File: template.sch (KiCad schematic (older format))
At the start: 24 parts, among them J1 power, J2 input, J3 output, J4 isp, K1 EC2-5NU, K2 EC2-5NU, K3 EC2-5NU, SW1 bypass switch, SW2 preset switch, U1 AMS1117-5.0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

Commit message: Lots of progress
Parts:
- D2, D3: footprint LED_THT:LED_D5.0mm -> LED_THT:LED_D5.0mm_compact
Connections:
- net 5V: now also K2.9; no longer K3.9
- net preset_2_in: now also K3.9; no longer K2.9
- net preset_2_out_a: now also K3.10; no longer K2.10
- net preset_2_out_b: now also K3.8; no longer K2.8
- net preset_led: now also K2.8; no longer K3.8
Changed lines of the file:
@@
 Text Label 4950 3250 0    50   ~ 0
 preset_switch
-Text Label 2100 7450 0    50   ~ 0
+Text Label 2100 6000 0    50   ~ 0
 preset_led
 Text Label 4950 3450 0    50   ~ 0
@@
 Text Label 1200 5500 2    50   ~ 0
 preset_1_in
-Text Label 1200 5900 2    50   ~ 0
+Text Label 1200 7350 2    50   ~ 0
 preset_2_in
 Wire Wire Line
 	1200 5500 1350 5500
 Wire Wire Line
-	1200 5900 1350 5900
+	1200 7350 1350 7350
 Text Label 10200 5200 0    50   ~ 0
 preset_1_in
@@
 	1200 6950 1350 6950
 Wire Wire Line
-	1200 7350 1350 7350
-Wire Wire Line
-	2100 7450 1950 7450
-NoConn ~ 1950 7250
+	1200 5900 1350 5900
+Wire Wire Line
+	2100 6000 1950 6000
+NoConn ~ 1950 5800
 Text Label 2100 7050 0    50   ~ 0
 preset_3_out_b
@@
 Wire Wire Line
 	8700 5750 8850 5750
-Text Label 2100 6000 0    50   ~ 0
+Text Label 2100 7450 0    50   ~ 0
 preset_2_out_b
 Wire Wire Line
-	2100 6000 1950 6000
-Text Label 2100 5800 0    50   ~ 0
+	2100 7450 1950 7450
+Text Label 2100 7250 0    50   ~ 0
 preset_2_out_a
 Wire Wire Line
-	2100 5800 1950 5800
+	2100 7250 1950 7250
 Text Label 8700 5450 2    50   ~ 0
 preset_2_out_a
@@
 Wire Wire Line
 	8850 5150 8700 5150
-Text Label 1200 7350 2    50   ~ 0
+Text Label 1200 5900 2    50   ~ 0
 5V
 $Comp
@@
 F 0 "D2" H 8043 1045 50  0000 C CNN
 F 1 "bypass" H 8043 1136 50  0000 C CNN
-F 2 "LED_THT:LED_D5.0mm" H 8050 1300 50  0001 C CNN
+F 2 "LED_THT:LED_D5.0mm_compact" H 8050 1300 50  0001 C CNN
 F 3 "~" H 8050 1300 50  0001 C CNN
 	1    8050 1300
@@
 F 0 "D3" H 8043 1995 50  0000 C CNN
 F 1 "preset" H 8043 2086 50  0000 C CNN
-F 2 "LED_THT:LED_D5.0mm" H 8050 2250 50  0001 C CNN
+F 2 "LED_THT:LED_D5.0mm_compact" H 8050 2250 50  0001 C CNN
 F 3 "~" H 8050 2250 50  0001 C CNN
 	1    8050 2250

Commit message: Some layout improvements
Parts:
- SW1, SW2: footprint Connector_JST:JST_XH_B2B-XH-AM_1x02_P2.50mm_Vertical -> Connector_JST:JST_XH_B2B-XH-A_1x02_P2.50mm_Vertical
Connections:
- net preset_relay: now also U3.5 (gate2); no longer U4.5 (gate2)
- net relay_3: now also U3.3 (drain2); no longer U4.3 (drain2)
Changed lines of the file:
@@
 F 0 "SW1" H 9200 1535 50  0000 C CNN
 F 1 "bypass switch" H 9200 1444 50  0000 C CNN
-F 2 "Connector_JST:JST_XH_B2B-XH-AM_1x02_P2.50mm_Vertical" H 9200 1300 50  0001 C CNN
+F 2 "Connector_JST:JST_XH_B2B-XH-A_1x02_P2.50mm_Vertical" H 9200 1300 50  0001 C CNN
 F 3 "~" H 9200 1300 50  0001 C CNN
 	1    9200 1300
@@
 F 0 "SW2" H 9200 2485 50  0000 C CNN
 F 1 "preset switch" H 9200 2394 50  0000 C CNN
-F 2 "Connector_JST:JST_XH_B2B-XH-AM_1x02_P2.50mm_Vertical" H 9200 2250 50  0001 C CNN
+F 2 "Connector_JST:JST_XH_B2B-XH-A_1x02_P2.50mm_Vertical" H 9200 2250 50  0001 C CNN
 F 3 "~" H 9200 2250 50  0001 C CNN
 	1    9200 2250
@@
 Wire Wire Line
 	3750 5200 3850 5200
-NoConn ~ 3850 5300
-NoConn ~ 4450 5000
 Text Label 5650 5200 2    50   ~ 0
 preset_relay
-Wire Wire Line
-	5650 5200 5750 5200
-Wire Wire Line
-	5750 5200 5750 5300
-Wire Wire Line
-	5750 5300 5800 5300
-Connection ~ 5750 5200
-Wire Wire Line
-	5750 5200 5800 5200
 Text Label 6300 4900 1    50   ~ 0
 relay_2
@@
 	6300 4900 6300 5000
 Wire Wire Line
-	6400 4900 6400 5000
-Text Label 6400 4900 1    50   ~ 0
+	4450 4900 4450 5000
+Text Label 4450 4900 1    50   ~ 0
 relay_3
 $Comp
@@
 	1    0    0    -1
 $EndComp
+Text Label 3750 5300 2    50   ~ 0
+preset_relay
+Wire Wire Line
+	3850 5300 3750 5300
+Wire Wire Line
+	5650 5200 5800 5200
+NoConn ~ 6400 5000
+NoConn ~ 5800 5300
 $EndSCHEMATC

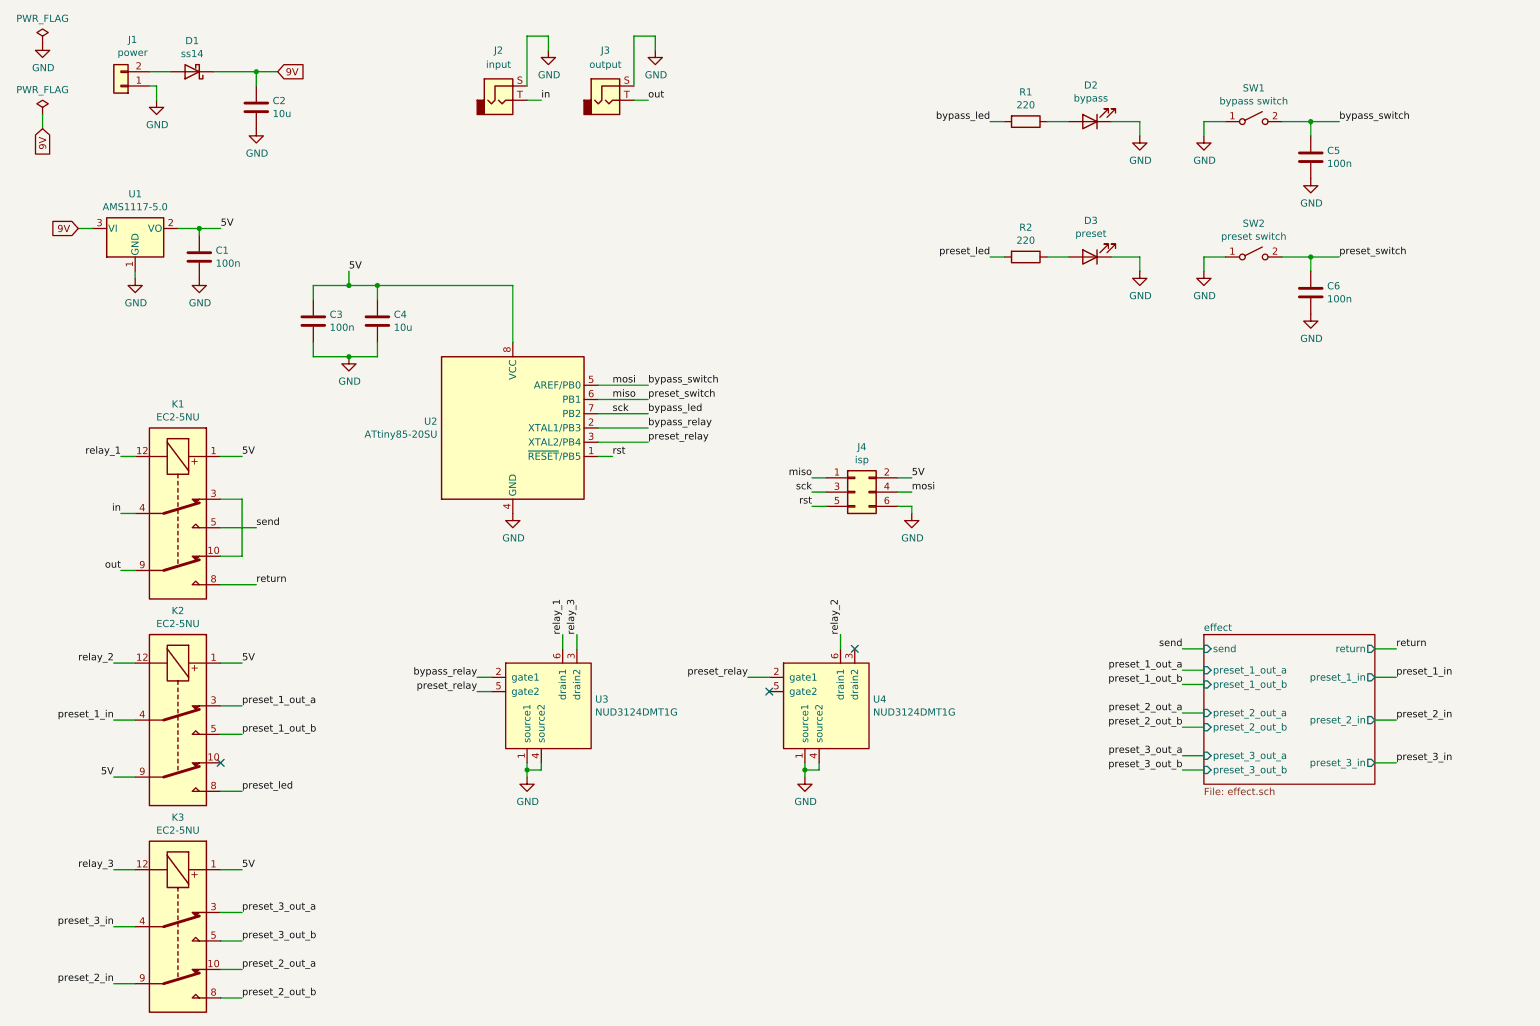
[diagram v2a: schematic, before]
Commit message: Use solid state switching and charge pump
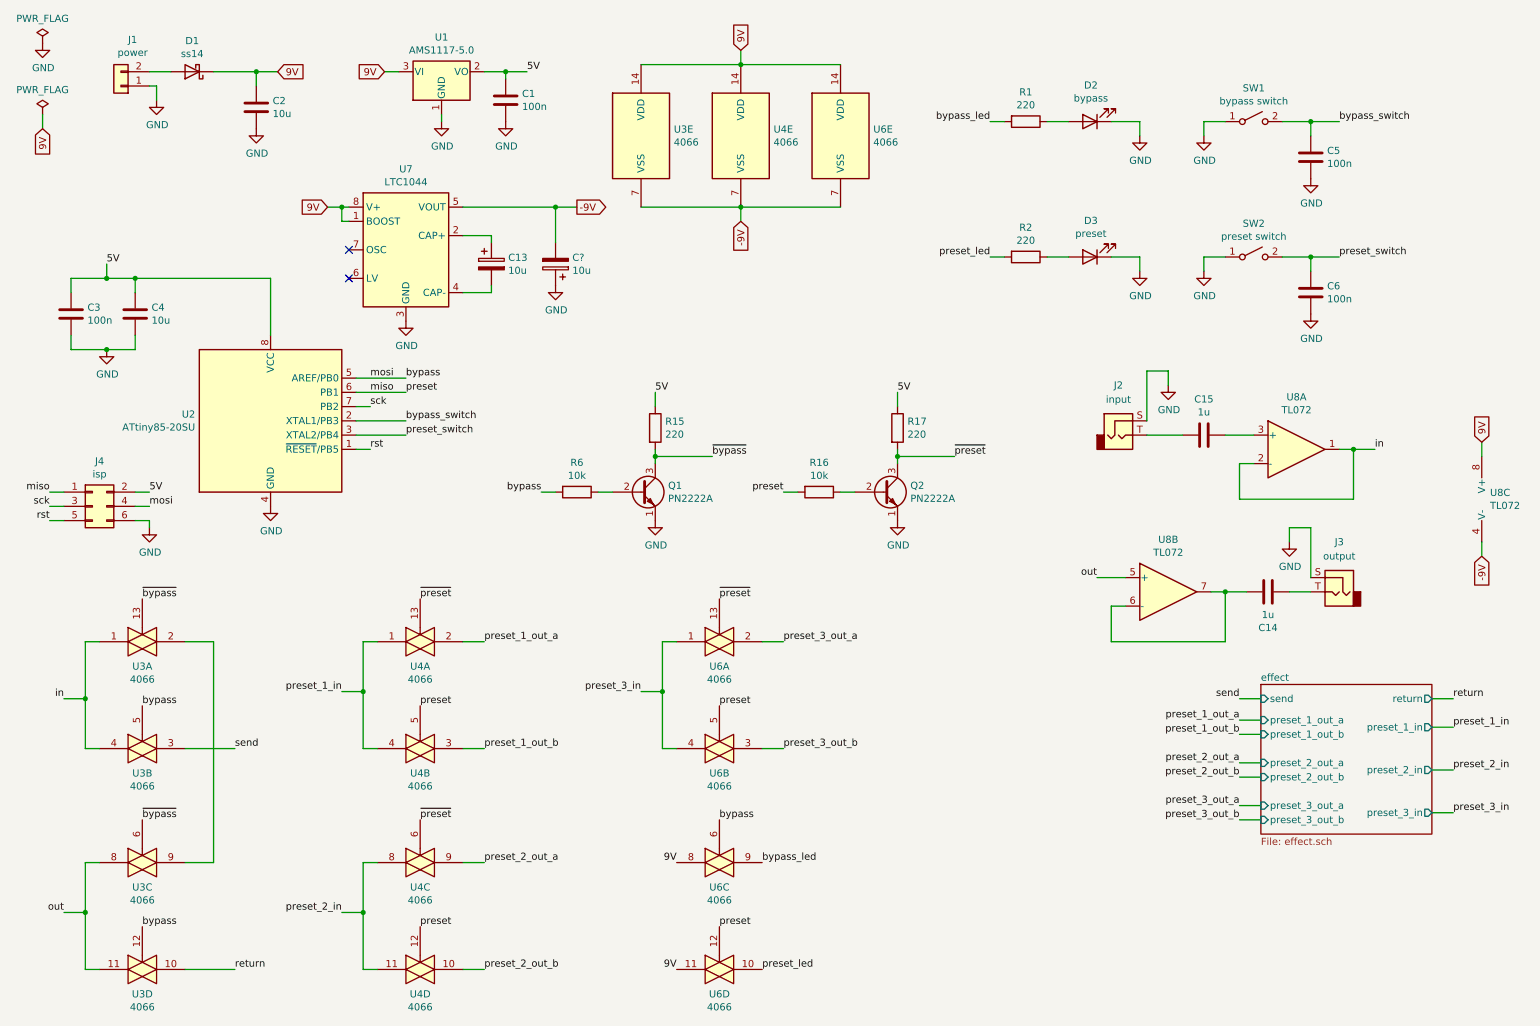
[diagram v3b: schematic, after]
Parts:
- removed K1, K2, K3: EC2-5NU, Relay_THT:Relay_DPDT_Kemet_EC2, symbol Relay:EC2-5NU
- removed U3, U4: NUD3124DMT1G, Package_SO:SC-74-6_1.5x2.9mm_P0.95mm, symbol Power_Management:NUD3124DMT1G
- added C13, C?: 10u, symbol Device:CP
- added C14, C15: 1u, symbol Device:C
- added Q1, Q2: PN2222A, Package_TO_SOT_THT:TO-92_Inline, symbol Transistor_BJT:PN2222A
- added R15, R17: 220, symbol Device:R
- added R16, R6: 10k, symbol Device:R
- added U3, U4, U6: 4066, symbol 4xxx:4066
- added U7: LTC1044, symbol Regulator_SwitchedCapacitor:LTC1044
- added U8: TL072, symbol Amplifier_Operational:TL072
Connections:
- net bypass_relay is gone; now on net bypass_switch: U2.2 (XTAL1/PB3)
- net 5V: now also R15.1, R17.1
- net 9V: now also U3.14 (VDD), U4.14 (VDD), U6.11, U6.14 (VDD), U6.8, U7.1 (BOOST), U7.8 (V+), U8.8 (V+)
- net GND: now also C?.1, Q1.1 (E), Q2.1 (E), U7.3 (GND)
- net bypass_led: now also U6.9; no longer J4.3 (Pin_3), U2.7 (PB2)
- net bypass_switch: no longer J4.4 (Pin_4), U2.5 (AREF/PB0)
- net in: now also U3.1, U3.4, U8.1, U8.2 (-); no longer J2.T
- net miso: now also R16.2, U4.12, U4.5, U6.12, U6.5; no longer C6.1, SW2.2 (B)
- net out: now also U3.11, U3.8, U8.5 (+); no longer J3.T
- net preset_1_in: now also U4.1, U4.4
- net preset_1_out_a: now also U4.2
- net preset_1_out_b: now also U4.3
- net preset_2_in: now also U4.11, U4.8
- net preset_2_out_a: now also U4.9
- net preset_2_out_b: now also U4.10
- net preset_3_in: now also U6.1, U6.4
- net preset_3_out_a: now also U6.2
- net preset_3_out_b: now also U6.3
- net preset_led: now also U6.10
- net return: now also U3.10
- net send: now also U3.3
- net preset_relay renamed preset_switch
- net preset_switch: now also C6.1, SW2.2 (B)
- new net: C15.2, J2.T
- new net: C14.2, J3.T
- new net: U3.2, U3.9
- new net: Q1.2 (B), R6.1
- new net: Q2.2 (B), R16.1
- new net: C14.1, U8.6 (-), U8.7
- new net: C15.1, U8.3 (+)
- new net: C13.1, U7.2 (CAP+)
- new net: C13.2, U7.4 (CAP-)
- new net -9V: C?.2, U3.7 (VSS), U4.7 (VSS), U6.7 (VSS), U7.5 (VOUT), U8.4 (V-)
- new net bypass: J4.4 (Pin_4), R6.2, U2.5 (AREF/PB0), U3.12, U3.5, U6.6
- new net sck: J4.3 (Pin_3), U2.7 (PB2)
- new net ~bypass: Q1.3 (C), R15.2, U3.13, U3.6
- new net ~preset: Q2.3 (C), R17.2, U4.13, U4.6, U6.13
- no-connect marks 3 -> 2
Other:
- moved on the sheet: C1, C3, C4, J2, J3, J4, U1, U2

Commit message: Use 4053 switch, correct poor decisions made earlier
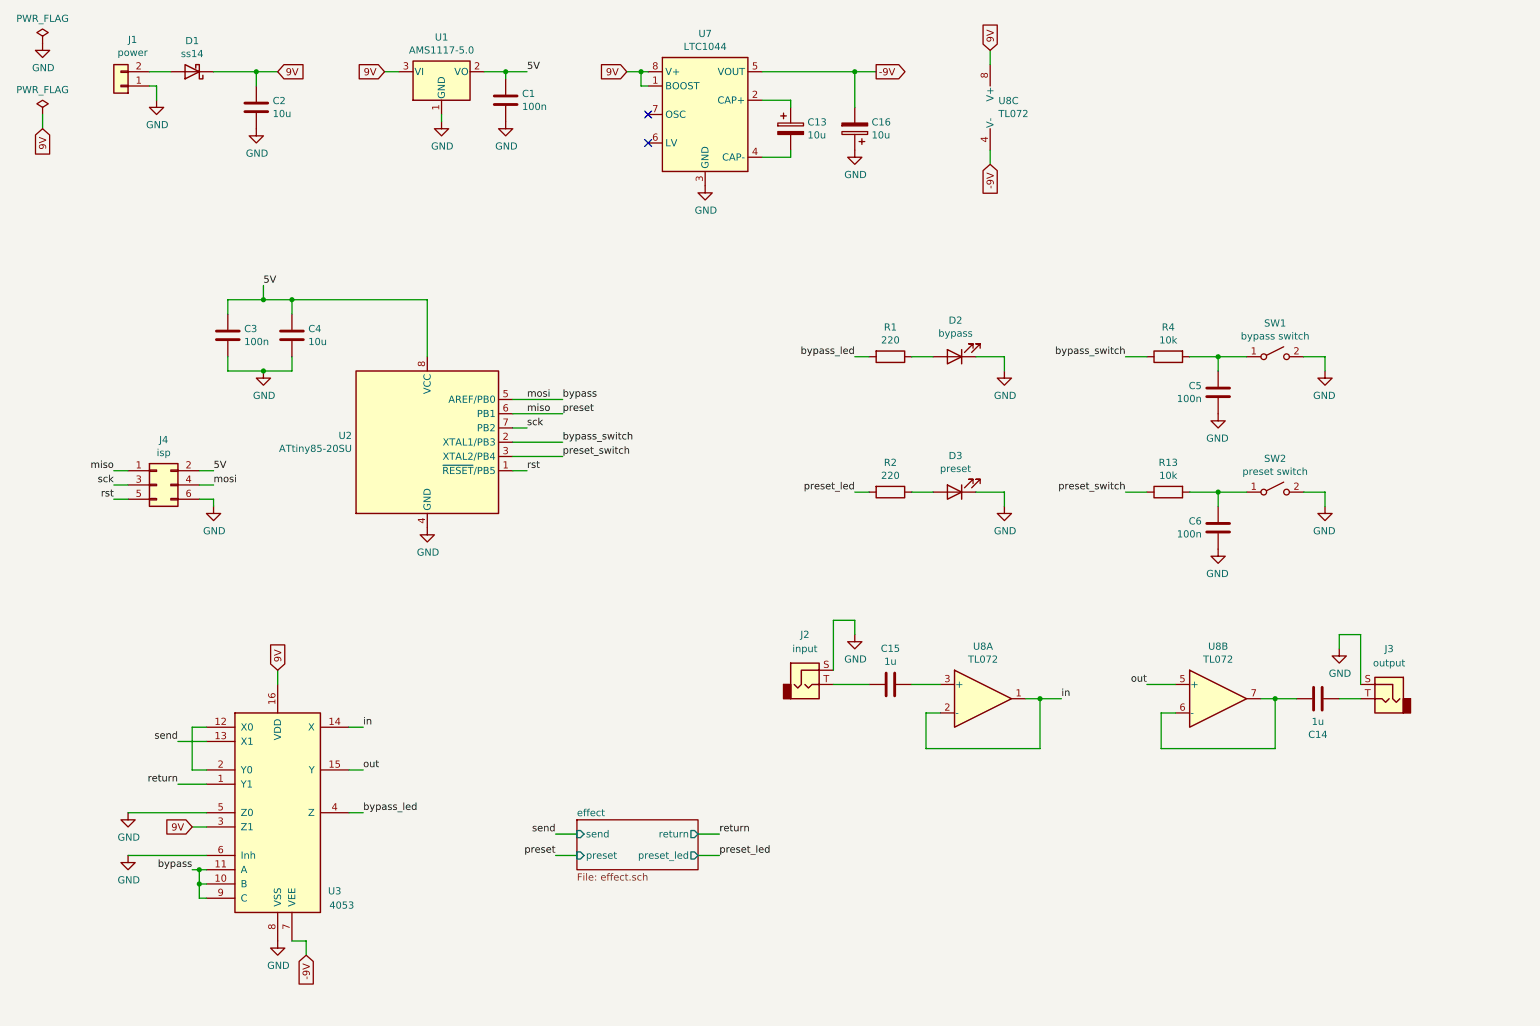
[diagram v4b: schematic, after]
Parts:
- removed Q1, Q2: PN2222A, Package_TO_SOT_THT:TO-92_Inline, symbol Transistor_BJT:PN2222A
- removed R15, R17: 220, symbol Device:R
- removed R16, R6: 10k, symbol Device:R
- removed U3, U4, U6: 4066, symbol 4xxx:4066
- added R13, R4: 10k, symbol Device:R
- added U3: 4053, symbol 4xxx:4053
- gave numbers to parts that had none: 1
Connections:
- net -9V: now also U3.7 (VEE)
- net 9V: now also U3.16 (VDD), U3.3 (Z1)
- net GND: now also SW1.2 (B), SW2.2 (B), U3.5 (Z0), U3.6 (Inh), U3.8 (VSS); no longer SW1.1 (A), SW2.1 (A)
- net bypass: now also U3.10 (B), U3.11 (A), U3.9 (C)
- net bypass_led: now also U3.4 (Z)
- net bypass_switch: now also R4.1; no longer C5.1, SW1.2 (B)
- net in: now also U3.14 (X)
- net out: now also U3.15 (Y)
- net preset_switch: now also R13.1; no longer C6.1, SW2.2 (B)
- net return: now also U3.1 (Y1)
- net send: now also U3.13 (X1)
- new net: C5.1, R4.2, SW1.1 (A)
- new net: C6.1, R13.2, SW2.1 (A)
- new net: U3.12 (X0), U3.2 (Y0)
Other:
- moved on the sheet: C13, C14, C15, C16, C3, C4, C5, C6, D2, D3, J2, J3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

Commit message: Fix a few issues
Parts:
- added Q1: MMBT3904, Package_TO_SOT_SMD:SOT-23, symbol Transistor_BJT:MMBT3904
- added R6: 10k, symbol Device:R
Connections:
- net preset_led is gone; now on net 9V: R2.2
- net GND: now also Q1.2 (E); no longer D3.1 (K)
- net miso: now also R6.2
- new net: D3.1 (K), Q1.3 (C)
- new net: Q1.1 (B), R6.1
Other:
- moved on the sheet: C5, C6, D2, D3, R1, R13, R2, R4, SW1, SW2

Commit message: Reformatting
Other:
- moved on the sheet: J2, J3
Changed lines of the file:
@@
 U 1 1 60CBEC11
 P 6050 5250
-F 0 "J2" H 6050 5600 50  0000 C CNN
-F 1 "input" H 6050 5500 50  0000 C CNN
+F 0 "J2" H 6050 4950 50  0000 C CNN
+F 1 "input" H 6050 5050 50  0000 C CNN
 F 2 "Connector_Audio:Jack_6.35mm_Neutrik_NMJ4HCD2_Horizontal" H 6050 5250 50  0001 C CNN
 F 3 "~" H 6050 5250 50  0001 C CNN
 	1    6050 5250
-	1    0    0    -1
+	1    0    0    1
 $EndComp
 Text Label 7850 5350 0    50   ~ 0
@@
 L power:GND #PWR09
 U 1 1 60CC3E5B
-P 6400 4900
-F 0 "#PWR09" H 6400 4650 50  0001 C CNN
-F 1 "GND" H 6405 4727 50  0000 C CNN
-F 2 "" H 6400 4900 50  0001 C CNN
-F 3 "" H 6400 4900 50  0001 C CNN
-	1    6400 4900
-	1    0    0    -1
-$EndComp
-Wire Wire Line
-	6250 5150 6250 4800
-Wire Wire Line
-	6250 4800 6400 4800
-Wire Wire Line
-	6400 4800 6400 4900
+P 6350 5400
+F 0 "#PWR09" H 6350 5150 50  0001 C CNN
+F 1 "GND" H 6355 5227 50  0000 C CNN
+F 2 "" H 6350 5400 50  0001 C CNN
+F 3 "" H 6350 5400 50  0001 C CNN
+	1    6350 5400
+	1    0    0    -1
+$EndComp
 $Comp
 L Connector:AudioJack2 J3
 U 1 1 60CC824C
 P 10150 5350
-F 0 "J3" H 10150 5700 50  0000 C CNN
-F 1 "output" H 10150 5600 50  0000 C CNN
+F 0 "J3" H 10150 5050 50  0000 C CNN
+F 1 "output" H 10150 5150 50  0000 C CNN
 F 2 "Connector_Audio:Jack_6.35mm_Neutrik_NMJ4HCD2_Horizontal" H 10150 5350 50  0001 C CNN
 F 3 "~" H 10150 5350 50  0001 C CNN
 	1    10150 5350
-	-1   0    0    -1
+	-1   0    0    1
 $EndComp
 Text Label 8450 5250 2    50   ~ 0
@@
 L power:GND #PWR010
 U 1 1 60CC8254
-P 9800 5000
-F 0 "#PWR010" H 9800 4750 50  0001 C CNN
-F 1 "GND" H 9805 4827 50  0000 C CNN
-F 2 "" H 9800 5000 50  0001 C CNN
-F 3 "" H 9800 5000 50  0001 C CNN
-	1    9800 5000
-	1    0    0    -1
-$EndComp
-Wire Wire Line
-	9950 5250 9950 4900
-Wire Wire Line
-	9800 4900 9800 5000
+P 9900 5500
+F 0 "#PWR010" H 9900 5250 50  0001 C CNN
+F 1 "GND" H 9905 5327 50  0000 C CNN
+F 2 "" H 9900 5500 50  0001 C CNN
+F 3 "" H 9900 5500 50  0001 C CNN
+	1    9900 5500
+	1    0    0    -1
+$EndComp
 $Comp
 L Connector_Generic:Conn_01x02 J1
@@
 U 1 1 60FF69D0
 P 9650 5350
-F 0 "C14" V 9398 5350 50  0000 C CNN
-F 1 "1u" V 9489 5350 50  0000 C CNN
+F 0 "C14" V 9900 5350 50  0000 C CNN
+F 1 "1u" V 9800 5350 50  0000 C CNN
 F 2 "" H 9688 5200 50  0001 C CNN
 F 3 "~" H 9650 5350 50  0001 C CNN
@@
 NoConn ~ 4950 1250
 NoConn ~ 4950 1450
-Wire Wire Line
-	9800 4900 9950 4900
 $Comp
 L Device:CP C16
@@
 Wire Wire Line
 	2950 5850 2850 5850
-Text GLabel 2550 7150 3    50   Input ~ 0
+Text GLabel 2550 7050 2    50   Input ~ 0
 -9V
 $Comp
@@
 Wire Wire Line
 	2450 7050 2550 7050
-Wire Wire Line
-	2550 7050 2550 7150
-Text GLabel 2350 5150 1    50   Input ~ 0
+Text GLabel 2350 5250 1    50   Input ~ 0
 9V
-Wire Wire Line
-	2350 5150 2350 5250
 $Comp
 L power:GND #PWR020
 U 1 1 610D2BF2
-P 1300 6450
-F 0 "#PWR020" H 1300 6200 50  0001 C CNN
-F 1 "GND" H 1305 6277 50  0000 C CNN
-F 2 "" H 1300 6450 50  0001 C CNN
-F 3 "" H 1300 6450 50  0001 C CNN
-	1    1300 6450
-	1    0    0    -1
-$EndComp
-Wire Wire Line
-	1300 6450 1850 6450
+P 1700 6350
+F 0 "#PWR020" H 1700 6100 50  0001 C CNN
+F 1 "GND" H 1550 6300 50  0000 C CNN
+F 2 "" H 1700 6350 50  0001 C CNN
+F 3 "" H 1700 6350 50  0001 C CNN
+	1    1700 6350
+	1    0    0    -1
+$EndComp
 Text GLabel 1750 6250 0    50   Input ~ 0
 9V
@@
 L power:GND #PWR011
 U 1 1 61093534
-P 1300 6150
-F 0 "#PWR011" H 1300 5900 50  0001 C CNN
-F 1 "GND" H 1305 5977 50  0000 C CNN
-F 2 "" H 1300 6150 50  0001 C CNN
-F 3 "" H 1300 6150 50  0001 C CNN
-	1    1300 6150
-	1    0    0    -1
-$EndComp
-Wire Wire Line
-	1300 6150 1850 6150
+P 1700 6050
+F 0 "#PWR011" H 1700 5800 50  0001 C CNN
+F 1 "GND" H 1550 6000 50  0000 C CNN
+F 2 "" H 1700 6050 50  0001 C CNN
+F 3 "" H 1700 6050 50  0001 C CNN
+	1    1700 6050
+	1    0    0    -1
+$EndComp
 Text Label 2950 6150 0    50   ~ 0
 bypass_led
@@
 	1    0    0    -1
 $EndComp
+Wire Wire Line
+	1700 6350 1850 6350
+Wire Wire Line
+	1850 6350 1850 6450
+Wire Wire Line
+	1700 6050 1850 6050
+Wire Wire Line
+	1850 6050 1850 6150
+Wire Wire Line
+	6350 5400 6350 5350
+Wire Wire Line
+	6350 5350 6250 5350
+Wire Wire Line
+	9900 5500 9900 5450
+Wire Wire Line
+	9900 5450 9950 5450
 $EndSCHEMATC
